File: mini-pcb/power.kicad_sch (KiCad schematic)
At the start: 8 parts, among them J3 Barrel_Jack_Switch, U1 LM1117DT-5.0, U2 OPA1664D

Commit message: almost done with mini pcb
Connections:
- net DGND is gone; now on net GND: U2.11 (V-)

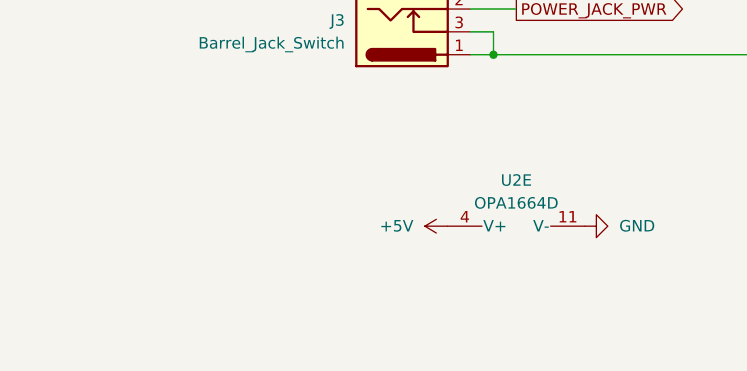
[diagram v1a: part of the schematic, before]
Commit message: made final touches and bom still needs through testing
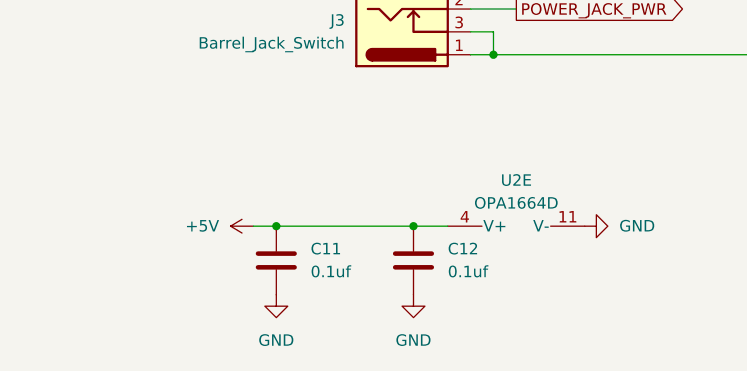
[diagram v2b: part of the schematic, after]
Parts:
- added C11, C12: 0.1uf, Capacitor_SMD:C_0805_2012Metric, symbol Device:C
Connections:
- net +5V: now also C11.1, C12.1
- net GND: now also C11.2, C12.2

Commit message: ordered pcb
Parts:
- removed C1, C4: 10UF, Capacitor_SMD:C_0805_2012Metric, symbol Device:C
- removed C11, C7: 0.1uf, Capacitor_SMD:C_0805_2012Metric, symbol Device:C
- added C1, C4: 10uf, Capacitor_Tantalum_SMD:CP_EIA-3216-18_Kemet-A, symbol Device:C_Polarized
- added C10: 0.1uf, Capacitor_SMD:C_0805_2012Metric, symbol Device:C
- added C18, C19: 1uf, Capacitor_SMD:C_0805_2012Metric, symbol Device:C
- added D2: LED, LED_SMD:LED_0805_2012Metric, symbol Device:LED
- added R27: 330, Resistor_SMD:R_0603_1608Metric, symbol Device:R
- added U4: LP5907MFX-2.5, Package_TO_SOT_SMD:SOT-23-5, symbol Regulator_Linear:LP5907MFX-2.5
- C12, C8: MPN (none) -> C49678
- D1: MPN (none) -> C8598
- J3: MPN (none) -> C16214
- U1: MPN (none) -> C354068
- U2: MPN (none) -> C69414
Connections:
- net +5V: now also C10.1, C18.1, C4.1, D2.2 (A), U4.1 (IN), U4.3 (EN)
- net +9V: now also C1.1
- net GND: now also C1.2, C10.2, C18.2, C19.2, C4.2, R27.1, U4.2 (GND)
- new net: D2.1 (K), R27.2
- new net +2.5V: C19.1, U4.5 (OUT)

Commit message: made mini-pcb report
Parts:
- removed C18, C19: 1uf, Capacitor_SMD:C_0805_2012Metric, symbol Device:C
- removed U4: LP5907MFX-2.5, Package_TO_SOT_SMD:SOT-23-5, symbol Regulator_Linear:LP5907MFX-2.5

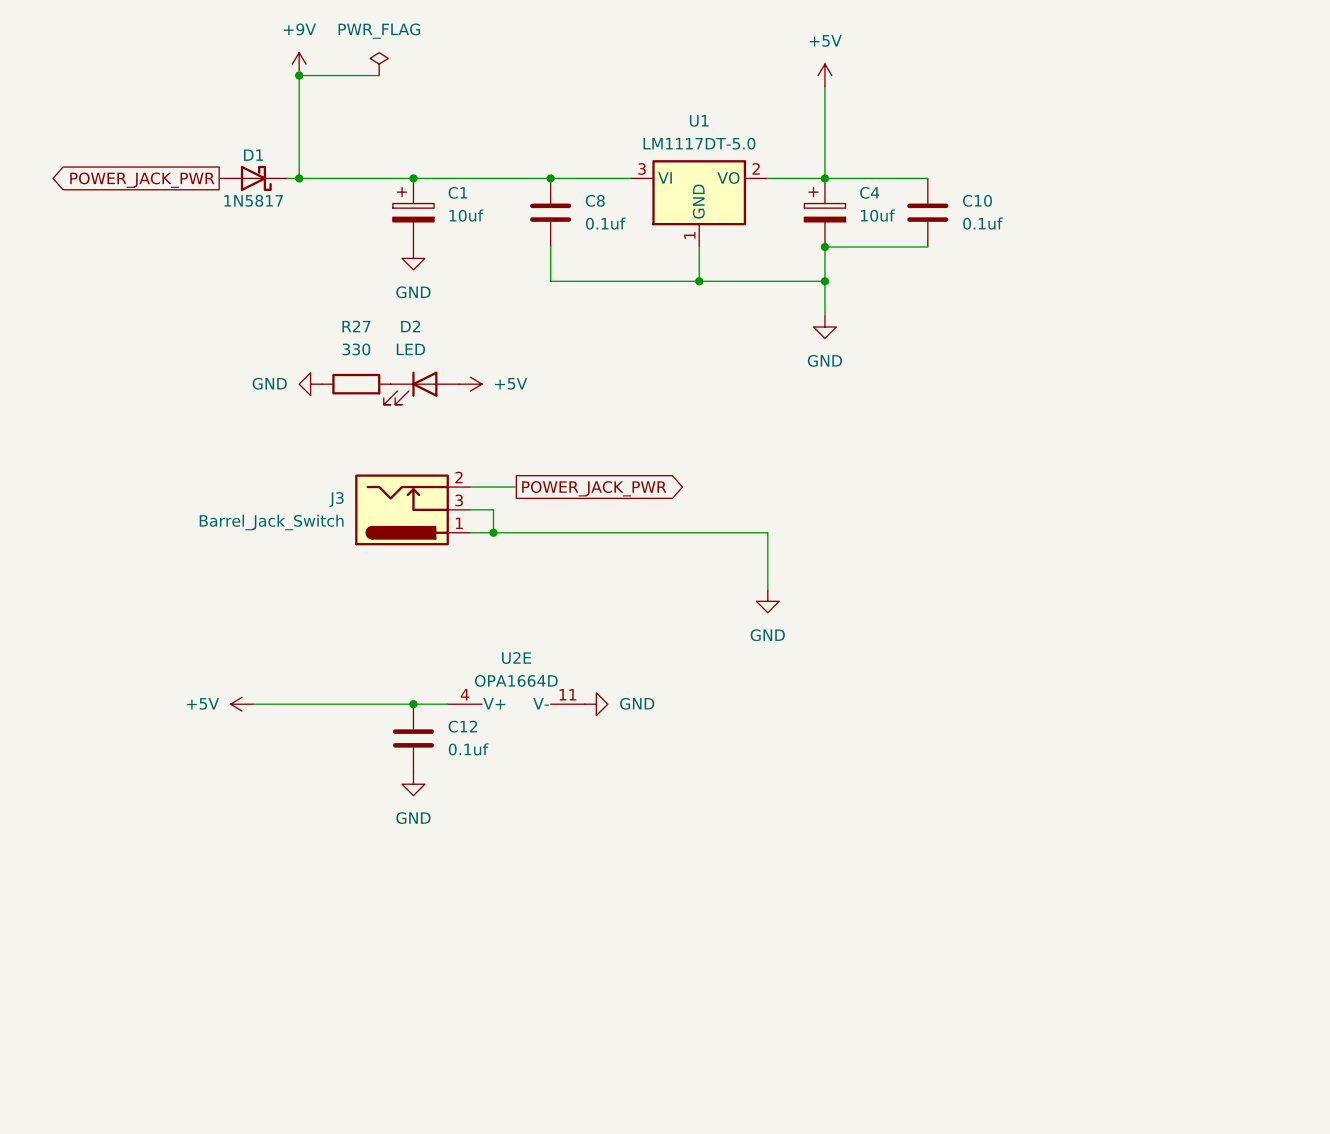
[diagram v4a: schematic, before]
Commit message: I will be re writing the code to use the daisy-embassy library because the Daisy one i have been using has a strange but crush effect when there is just a normal passthrough but the daisy-embassy example works well with my PCB also there was a testing problem earlyer with the PCB and the PCB works fine with no changes
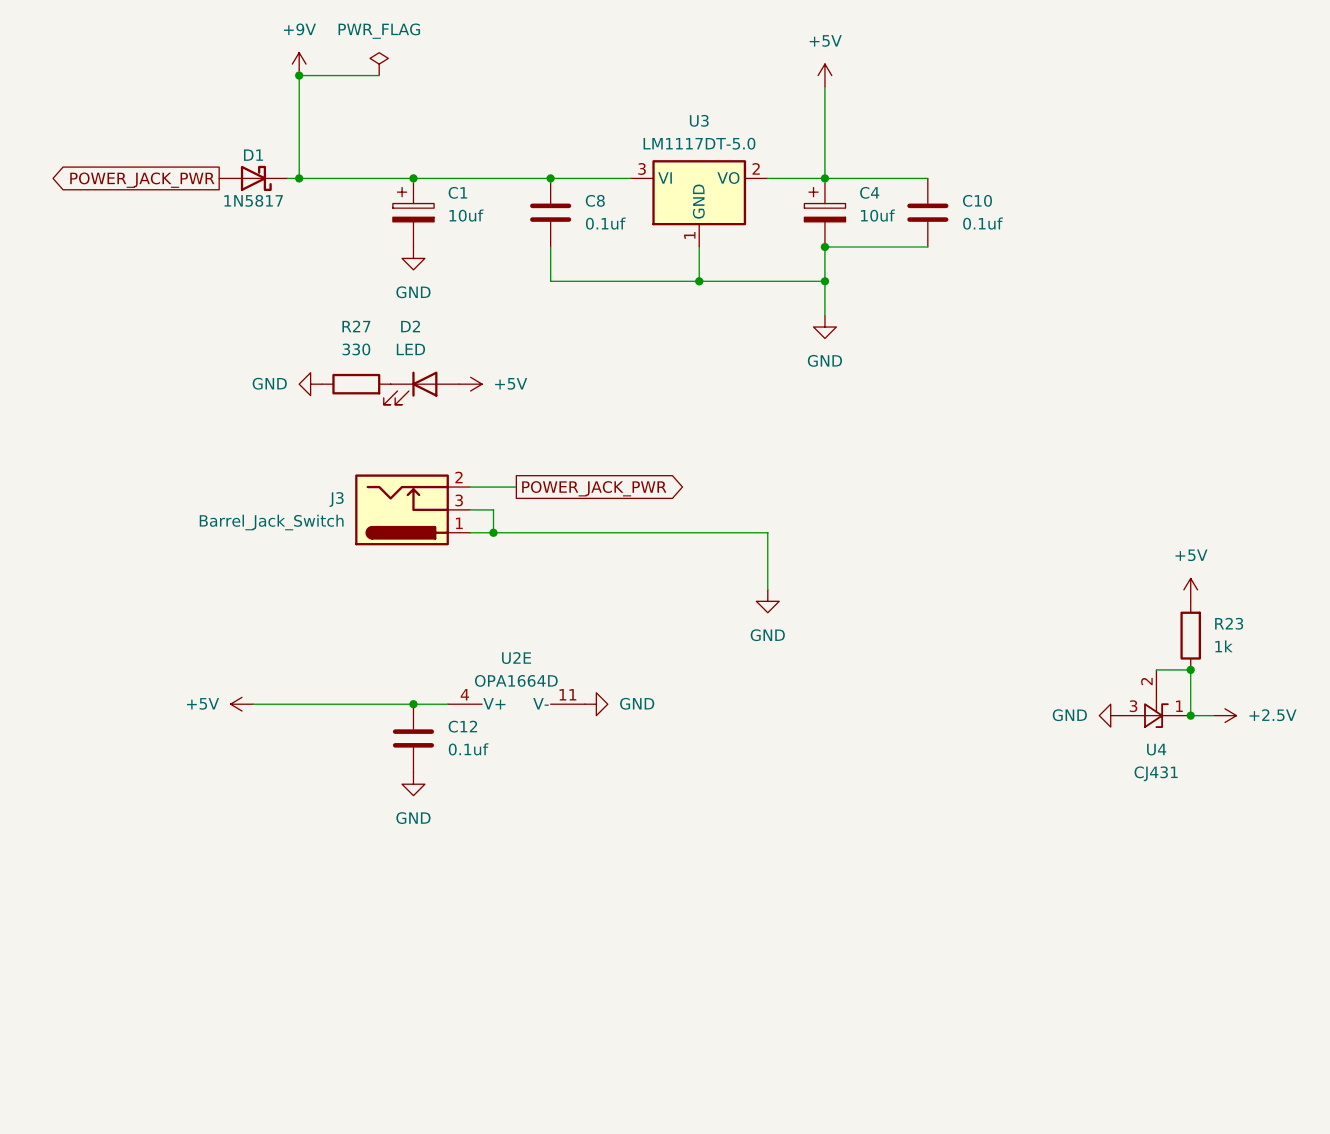
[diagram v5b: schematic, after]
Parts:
- removed U1: LM1117DT-5.0, Package_TO_SOT_SMD:TO-252-3_TabPin2, symbol Regulator_Linear:LM1117DT-5.0
- added R23: 1k, Resistor_SMD:R_0603_1608Metric, symbol Device:R
- added U3: LM1117DT-5.0, Package_TO_SOT_SMD:TO-252-2, symbol Regulator_Linear:LM1117DT-5.0
- added U4: CJ431, Package_TO_SOT_SMD:SOT-23-3, symbol Reference_Voltage:LM285Z-ADJ
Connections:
- net +5V: now also R23.2, U3.2 (VO)
- net +9V: now also U3.3 (VI)
- net GND: now also U3.1 (GND), U4.3 (A)
- new net +2.5V: R23.1, U4.1 (FB), U4.2 (K)
